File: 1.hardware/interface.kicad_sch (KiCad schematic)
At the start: 36 parts, among them J1 Conn_01x02, J12 Conn_01x02, J13 Conn_01x02, J14 Conn_01x03, J16 Can_conn, J7 uart_comm, J8 USB_C, SW1 Esp32_Btn, U11 SN65HVD230, U5 ESP32-C3-WROOM-02

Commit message: 중간 수정
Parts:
- removed J16: Can_conn, symbol Connector_Generic:Conn_01x02
- added J15: Can_conn, symbol Connector_Generic:Conn_01x06
- added J16: Conn_01x04, symbol Connector_Generic:Conn_01x04
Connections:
- net +3.3V: now also J16.1 (Pin_1)
- net CANH: now also J15.3 (Pin_3)
- net CANL: now also J15.4 (Pin_4)
- net GND: now also J16.4 (Pin_4)
- new net GNDPWR: J15.5 (Pin_5), J15.6 (Pin_6)
- new net I2C1_SCL: J16.3 (Pin_3)
- new net I2C1_SDA: J16.2 (Pin_2)
- new net PWR_INPUT(5V~24V): J15.1 (Pin_1), J15.2 (Pin_2)
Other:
- note removed: "CAN"

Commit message: 중간 저장
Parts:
- removed C62: 0.1uF/16V, Capacitor_SMD:C_0402_1005Metric, symbol Device:C_Small_US
- removed SW1: Esp32_Btn, symbol Switch:SW_Push
- added J9: Conn_01x02, symbol Connector_Generic:Conn_01x02
- added R138: 4.7K/0.063w, Resistor_SMD:R_0402_1005Metric, symbol Device:R_Small_US
- added S2: TSB008A2518A, SamacSys_Parts:TSB008A2518A, symbol SamacSys_Parts:TSB008A2518A
- LED3: value LED_0603_Red_WIFI -> LED_0603_Red
- R101, R105: value 4.7K/0.063w -> 0R/0.063w; footprint Resistor_SMD:R_0402_1005Metric -> (none)
- R107: value 4.7K/0.063w -> 10k/0.063w; footprint Resistor_SMD:R_0402_1005Metric -> (none)
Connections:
- net 3V3_MCU: now also R107.2
- net GND: now also J9.2 (Pin_2), S2.2 (NO); no longer U5.15 (IO3)
- net at J1.1 (Pin_1), R102.1, R103.1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: now also R138.1; no longer R101.1, R105.1, R107.1
- net at U5.13 (IO18): now also R105.2; no longer J12.2 (Pin_2)
- net at U5.14 (IO19): now also R101.2; no longer J13.1 (Pin_1)
- net ESP_EN: now reaches U5.2 (EN)
- net ESP_EN: now also R107.1, S2.1 (COM); no longer R101.2
- net at LED3.1 (K): now also U5.15 (IO3); no longer U5.8 (IO9)
- net at LED3.2 (A): now also R138.2; no longer R105.2
- new net: J13.1 (Pin_1), R101.1
- new net: J12.2 (Pin_2), R105.1
- new net ESP_BOOT: J9.1 (Pin_1), U5.8 (IO9)
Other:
- moved on the sheet: J12, J13, LED4, LED5, R102, R106

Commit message: 중간 저장
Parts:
- R102, R103, R104, R106, R138, R90, R91: value 4.7K/0.063w -> 4.7k/0.063w
- R115: value 120R -> 120/0.125w
- R92: value NC_4.7K -> NC_4.7k/0.1w
- R93: value 4.7K -> 4.7k/0.1w
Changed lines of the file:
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@@
 			)
 		)
-		(property "Value" "4.7K/0.063w"
+		(property "Value" "4.7k/0.063w"
 			(at 169.164 118.618 0)
 			(effects
@@
 			)
 		)
-		(property "Value" "4.7K/0.063w"
+		(property "Value" "4.7k/0.063w"
 			(at 56.642 84.582 0)
 			(effects
@@
 			)
 		)
-		(property "Value" "4.7K/0.063w"
+		(property "Value" "4.7k/0.063w"
 			(at 76.454 121.92 0)
 			(effects
@@
 			)
 		)
-		(property "Value" "4.7K/0.063w"
+		(property "Value" "4.7k/0.063w"
 			(at 149.86 118.364 0)
 			(effects
@@
 			)
 		)
-		(property "Value" "4.7K/0.063w"
+		(property "Value" "4.7k/0.063w"
 			(at 43.18 84.836 0)
 			(effects
@@
 			)
 		)
-		(property "Value" "4.7K/0.063w"
+		(property "Value" "4.7k/0.063w"
 			(at 55.626 121.666 0)
 			(effects
@@
 			)
 		)
-		(property "Value" "4.7K/0.063w"
+		(property "Value" "4.7k/0.063w"
 			(at 27.432 120.142 0)
 			(effects
@@
 			)
 		)
-		(property "Value" "120R"
+		(property "Value" "120/0.125w"
 			(at 160.02 62.2299 0)
 			(effects
@@
 			)
 		)
-		(property "Value" "4.7K"
-			(at 74.93 36.576 0)
+		(property "Value" "4.7k/0.1w"
+			(at 79.502 36.576 0)
 			(effects
 				(font
@@
 			)
 		)
-		(property "Value" "NC_4.7K"
+		(property "Value" "NC_4.7k/0.1w"
 			(at 72.898 29.972 0)
 			(effects

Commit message: 중간 저장
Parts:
- removed J1: Conn_01x02, symbol Connector_Generic:Conn_01x02
- J12: value Conn_01x02 -> ESP_DM_COMM
- J13: value Conn_01x02 -> ESP_DP_COMM
- J14: value Conn_01x03 -> ESP_DBG
- J9: value Conn_01x02 -> ESP_BOOT_CONN
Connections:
- net 3V3_MCU: now also R102.1, R103.1, R104.1, R106.1, R138.1, U5.1 (3V3)
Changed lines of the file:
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@@
 	(wire
 		(pts
-			(xy 172.72 113.03) (xy 185.42 113.03)
-		)
-		(stroke
-			(width 0)
-			(type default)
-		)
-	)
-	(wire
-		(pts
 			(xy 203.2 50.8) (xy 222.25 50.8)
 		)
@@
 	(wire
 		(pts
-			(xy 161.29 113.03) (xy 170.18 113.03)
+			(xy 161.29 113.03) (xy 185.42 113.03)
 		)
 		(stroke
@@
 	)
 	(symbol
-		(lib_id "Connector_Generic:Conn_01x02")
-		(at 170.18 107.95 90)
-		(unit 1)
-		(exclude_from_sim no)
-		(in_bom yes)
-		(on_board yes)
-		(dnp no)
-		(fields_autoplaced yes)
-		(property "Reference" "J1"
-			(at 175.26 106.6799 90)
-			(effects
-				(font
-					(size 1.27 1.27)
-				)
-				(justify right)
-			)
-		)
-		(property "Value" "Conn_01x02"
-			(at 175.26 109.2199 90)
-			(effects
-				(font
-					(size 1.27 1.27)
-				)
-				(justify right)
-			)
-		)
-		(property "Footprint" ""
-			(at 170.18 107.95 0)
-			(effects
-				(font
-					(size 1.27 1.27)
-				)
-				(hide yes)
-			)
-		)
-		(property "Datasheet" "~"
-			(at 170.18 107.95 0)
-			(effects
-				(font
-					(size 1.27 1.27)
-				)
-				(hide yes)
-			)
-		)
-		(property "Description" "Generic connector, single row, 01x02, script generated (kicad-library-utils/schlib/autogen/connector/)"
-			(at 170.18 107.95 0)
-			(effects
-				(font
-					(size 1.27 1.27)
-				)
-				(hide yes)
-			)
-		)
-		(pin "2"
-		)
-		(pin "1"
-		)
-		(instances
-			(project ""
-				(path "/a25adab6-a8c3-4e0e-8ba9-baac00aaa394/430b6e73-4ab5-4f88-adfd-520e070c0b15"
-					(reference "J1")
-					(unit 1)
-				)
-			)
-		)
-	)
-	(symbol
 		(lib_id "power:+3.3V")
 		(at 121.92 54.61 0)
@@
 			)
 		)
-		(property "Value" "Conn_01x03"
+		(property "Value" "ESP_DBG"
 			(at 173.99 128.2699 0)
 			(effects
@@
 			)
 		)
-		(property "Value" "Conn_01x02"
+		(property "Value" "ESP_DP_COMM"
 			(at 44.45 167.64 90)
 			(effects
@@
 			)
 		)
-		(property "Value" "Conn_01x02"
+		(property "Value" "ESP_BOOT_CONN"
 			(at 109.22 172.72 90)
 			(effects
@@
 			)
 		)
-		(property "Value" "Conn_01x02"
+		(property "Value" "ESP_DM_COMM"
 			(at 44.196 149.606 90)
 			(effects

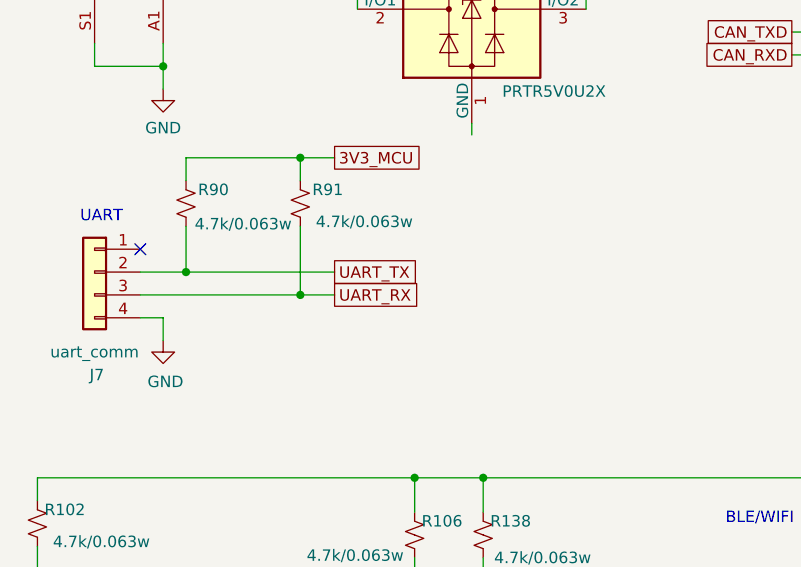
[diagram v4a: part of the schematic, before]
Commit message: 핀 배치 반영
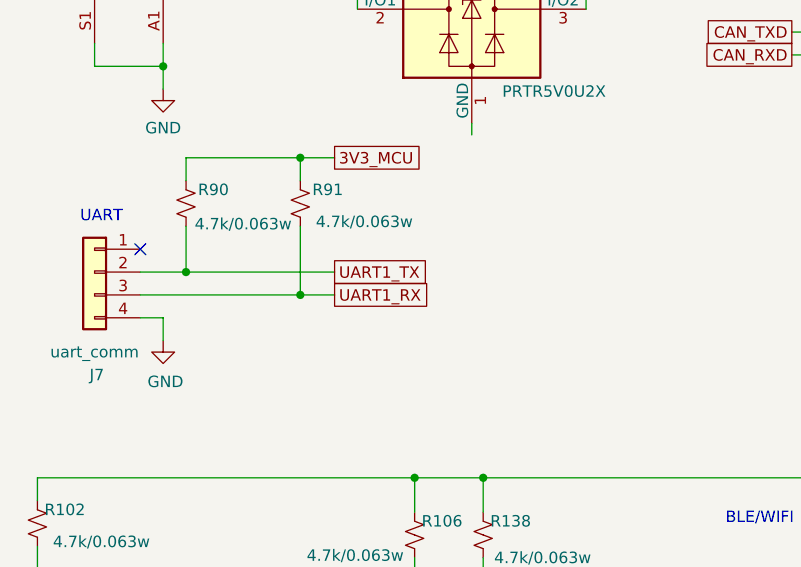
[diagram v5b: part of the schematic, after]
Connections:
- net UART_RX renamed UART1_RX
- net UART_TX renamed UART1_TX
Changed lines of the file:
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@@
 		)
 	)
-	(global_label "UART_TX"
+	(global_label "UART1_TX"
 		(shape passive)
 		(at 53.34 90.17 0)
@@
 		)
 		(property "Intersheetrefs" "${INTERSHEET_REFS}"
-			(at 63.0153 90.17 0)
+			(at 64.2248 90.17 0)
 			(effects
 				(font
@@
 		)
 	)
-	(global_label "UART_RX"
+	(global_label "UART1_RX"
 		(shape passive)
 		(at 53.34 92.71 0)
@@
 		)
 		(property "Intersheetrefs" "${INTERSHEET_REFS}"
-			(at 63.3177 92.71 0)
-			(effects
-				(font
+			(at 64.5272 92.71 0)
+			(effects
+				(font

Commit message: 중간 저장
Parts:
- C57: renamed from C50; value 0.1uF/16V -> 0.1uF/50V; footprint Capacitor_SMD:C_0402_1005Metric -> Capacitor_SMD:C_0603_1608Metric
- C58: renamed from C51; value 0.1uF/16V -> 0.1uF/50V; footprint Capacitor_SMD:C_0402_1005Metric -> Capacitor_SMD:C_0603_1608Metric
- C59: renamed from C70; value 0.1uF/16V -> 0.1uF/50V; footprint Capacitor_SMD:C_0402_1005Metric -> Capacitor_SMD:C_0603_1608Metric
- C61: renamed from C71; value 0.1uF/16V -> 0.1uF/50V; footprint Capacitor_SMD:C_0402_1005Metric -> Capacitor_SMD:C_0603_1608Metric
- R39: renamed from R107; footprint (none) -> Resistor_SMD:R_0402_1005Metric
- R44: renamed from R105; footprint (none) -> Resistor_SMD:R_0402_1005Metric
- R45: renamed from R101; footprint (none) -> Resistor_SMD:R_0402_1005Metric
- R46: renamed from R115; footprint (none) -> Resistor_SMD:R_0805_2012Metric
- R49: renamed from R118; footprint (none) -> Resistor_SMD:R_0402_1005Metric
- renumbered C52 to C60, D11 to D10, D12 to D11, J16 to J10, J14 to J11, J7 to J4, J8 to J5, J12 to J6, J13 to J7, J9 to J8, J15 to J9, LED5 to LED3, LED3 to LED5, R102 to R36, R90 to R37, R91 to R38, R106 to R40, R138 to R41, R92 to R42, R93 to R43, R103 to R47, R104 to R48, S2 to S3, U11 to U3, U5 to U4
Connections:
- net 3V3_MCU: no longer C57.1, C58.1, C60.1, R36.1, R40.1, R41.1, R47.1, R48.1, U4.1 (3V3)
- net GND: now also D9.1 (GND)
- net ESP32_SPI2_MISO renamed ESP32_SPI1_MISO
- net ESP32_SPI2_MOSI renamed ESP32_SPI1_MOSI
- net ESP32_SPI2_NSS renamed ESP32_SPI1_NSS
- net ESP32_SPI2_SCK renamed ESP32_SPI1_SCK
- new net 3V3_ESP32: C57.1, C58.1, C60.1, R36.1, R40.1, R41.1, R47.1, R48.1, U4.1 (3V3)

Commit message: 중간 저장
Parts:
- removed J6: ESP_DM_COMM, symbol Connector_Generic:Conn_01x02
- removed J7: ESP_DP_COMM, symbol Connector_Generic:Conn_01x02
- added J15: CAN_CONN2, symbol Connector_Generic:Conn_01x04
- J10: value Conn_01x04 -> I2C_CONN
- J11: value ESP_DBG -> ESP_DBG_CONN
- J4: value uart_comm -> UART_CONN
- J9: value Can_conn -> CAN_CONN
- R44, R45: value 0R/0.063w -> NC_0R/0.063w
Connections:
- net CANH: now also J15.2 (Pin_2)
- net CANL: now also J15.3 (Pin_3)
- net GNDPWR: now also J15.4 (Pin_4)
- net PWR_INPUT(5V~24V): now also J15.1 (Pin_1)
- net USB_DM: now also R44.1
- net USB_DP: now also R45.1

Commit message: 풋프린트 연결 완료
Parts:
- J10, J15, J4: footprint (none) -> Connector_PinSocket_2.54mm:PinSocket_1x04_P2.54mm_Vertical
- J11: footprint (none) -> Connector_PinSocket_2.54mm:PinSocket_1x03_P2.54mm_Vertical
- J8: footprint (none) -> Connector_PinHeader_2.54mm:PinHeader_1x02_P2.54mm_Vertical
- J9: footprint (none) -> Connector_JST:JST_SH_SM06B-SRSS-TB_1x06-1MP_P1.00mm_Horizontal
- S3: footprint SamacSys_Parts:TSB008A2518A -> SamacSys_Parts_Project:TSB008A2518A
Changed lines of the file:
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@@
 			)
 		)
-		(property "Footprint" "SamacSys_Parts:TSB008A2518A"
+		(property "Footprint" "SamacSys_Parts_Project:TSB008A2518A"
 			(at 72.39 177.8 0)
 			(effects
@@
 			)
 		)
-		(property "Footprint" ""
+		(property "Footprint" "Connector_PinSocket_2.54mm:PinSocket_1x03_P2.54mm_Vertical"
 			(at 171.45 127 0)
 			(effects
@@
 			)
 		)
-		(property "Footprint" ""
+		(property "Footprint" "Connector_JST:JST_SH_SM06B-SRSS-TB_1x06-1MP_P1.00mm_Horizontal"
 			(at 119.38 30.48 0)
 			(effects
@@
 			)
 		)
-		(property "Footprint" ""
+		(property "Footprint" "Connector_PinHeader_2.54mm:PinHeader_1x02_P2.54mm_Vertical"
 			(at 105.41 175.26 0)
 			(effects
@@
 			)
 		)
-		(property "Footprint" ""
+		(property "Footprint" "Connector_PinSocket_2.54mm:PinSocket_1x04_P2.54mm_Vertical"
 			(at 26.67 90.17 0)
 			(effects
@@
 			)
 		)
-		(property "Footprint" ""
+		(property "Footprint" "Connector_PinSocket_2.54mm:PinSocket_1x04_P2.54mm_Vertical"
 			(at 166.37 31.75 0)
 			(effects
@@
 			)
 		)
-		(property "Footprint" ""
+		(property "Footprint" "Connector_PinSocket_2.54mm:PinSocket_1x04_P2.54mm_Vertical"
 			(at 203.2 31.75 0)
 			(effects
